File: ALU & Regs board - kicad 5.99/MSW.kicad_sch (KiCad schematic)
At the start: 8 parts, among them U12 MC74ACT04DG, U19 MC74ACT08DG, U23 MC74ACT74DG, U24 MC74ACT74DG, U25 MC74ACT244DWG, U26 MC74ACT273DWG, U27 MC74ACT157DG, U28 MC74ACT244DWG

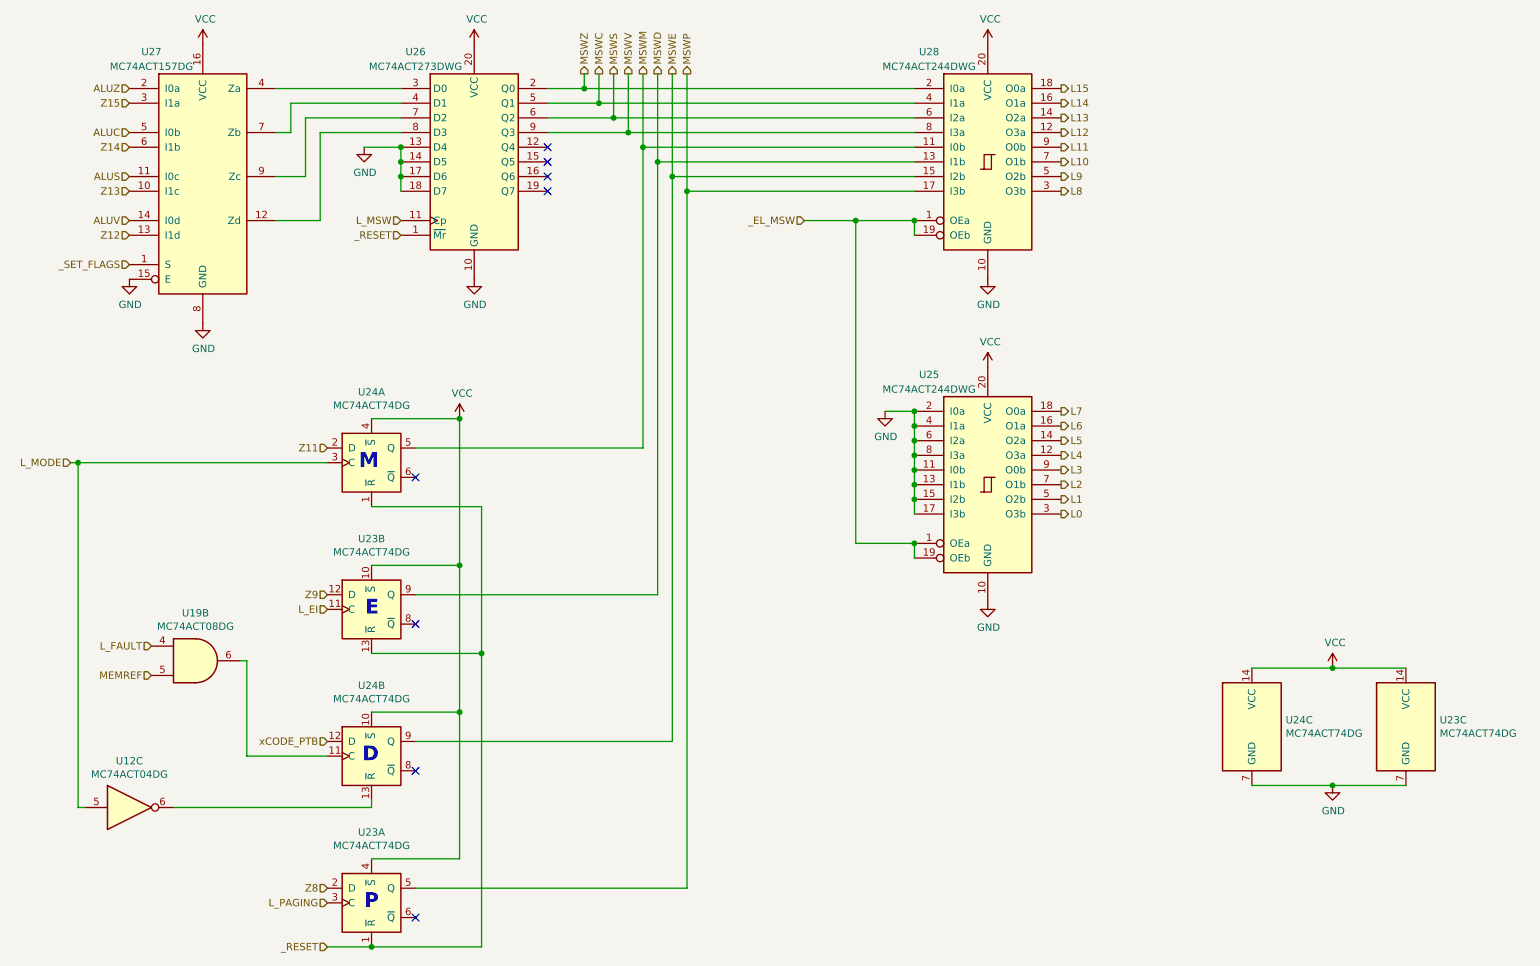
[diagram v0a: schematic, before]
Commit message: added a buffer on the _RESET line, which is rather loaded
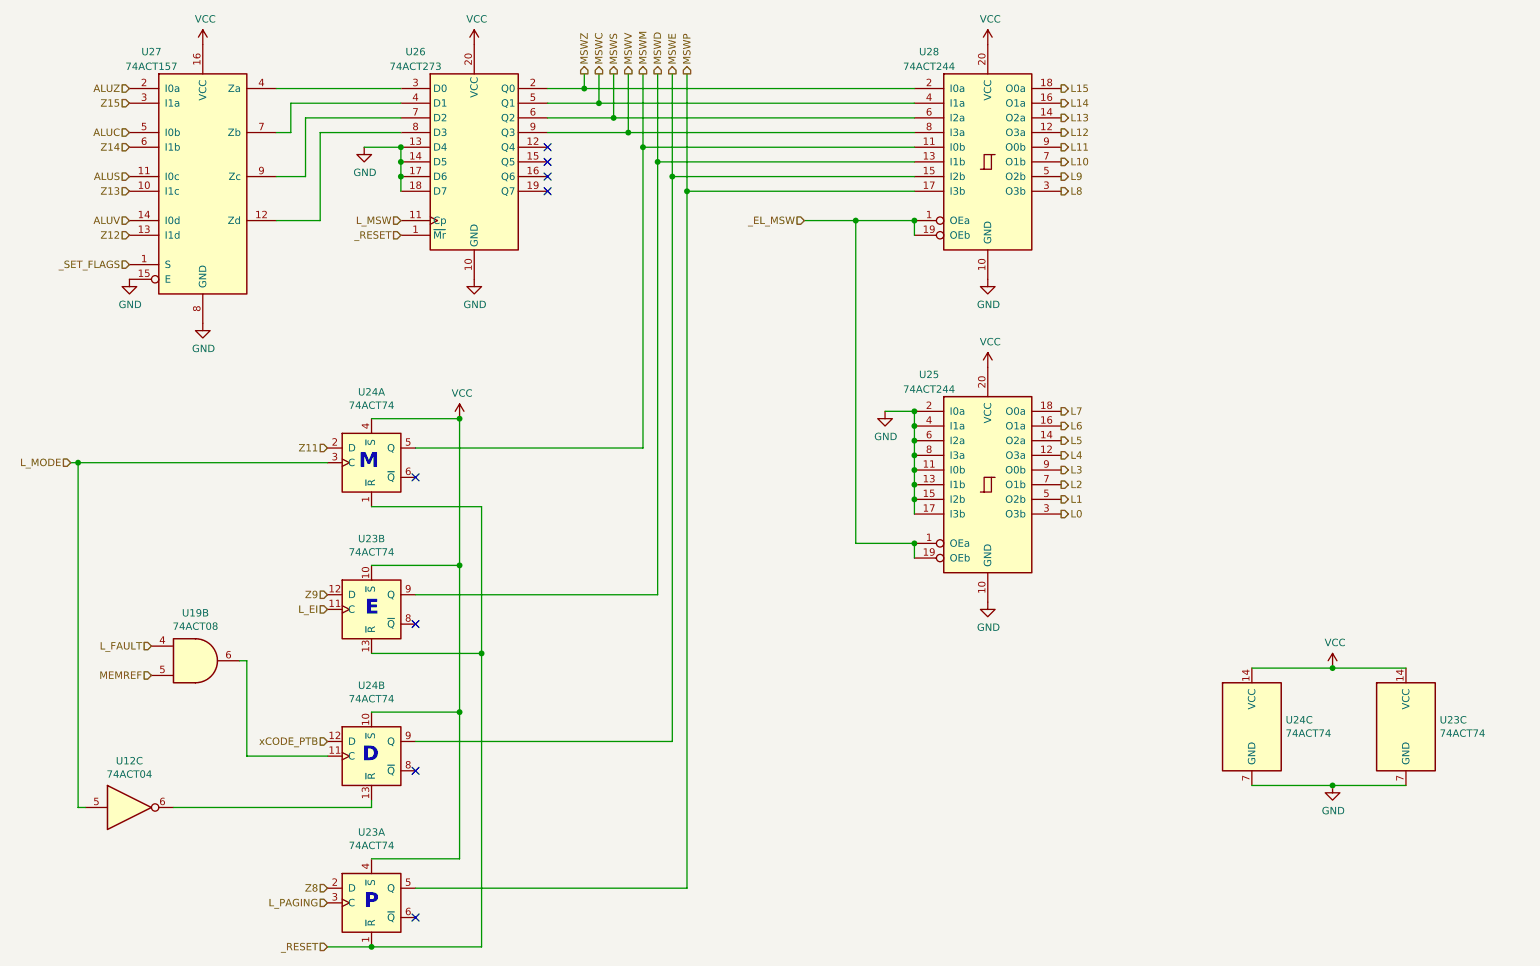
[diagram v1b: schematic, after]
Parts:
- U12: value MC74ACT04DG -> 74ACT04
- U19: value MC74ACT08DG -> 74ACT08
- U23, U24: value MC74ACT74DG -> 74ACT74
- U25, U28: value MC74ACT244DWG -> 74ACT244
- U26: value MC74ACT273DWG -> 74ACT273
- U27: value MC74ACT157DG -> 74ACT157
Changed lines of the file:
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@@
   (junction (at 245.11 134.62) (diameter 1.016) (color 0 0 0 0))
   (junction (at 245.11 154.94) (diameter 1.016) (color 0 0 0 0))
-  (no_connect (at 86.36 127))
+  (no_connect (at 86.36 152.4))
+  (no_connect (at 109.22 46.99))
+  (no_connect (at 109.22 49.53))
   (no_connect (at 109.22 44.45))
-  (no_connect (at 109.22 52.07))
-  (no_connect (at 109.22 49.53))
   (no_connect (at 86.36 101.6))
   (no_connect (at 86.36 177.8))
-  (no_connect (at 109.22 46.99))
-  (no_connect (at 86.36 152.4))
+  (no_connect (at 109.22 52.07))
+  (no_connect (at 86.36 127))
   (wire (pts (xy 27.94 99.06) (xy 26.67 99.06))
     (stroke (width 0) (type solid) (color 0 0 0 0))
@@
     (in_bom yes) (on_board yes)
     (property "Reference" "U12" (id 0) (at 36.83 150.6982 0))
-    (property "Value" "MC74ACT04DG" (id 1) (at 36.83 153.0096 0))
+    (property "Value" "74ACT04" (id 1) (at 36.83 153.01 0))
     (property "Footprint" "Package_SO:SOIC-14_3.9x8.7mm_P1.27mm" (id 2) (at 36.83 158.75 0)
       (effects (font (size 1.27 1.27)) hide)
@@
     (in_bom yes) (on_board yes)
     (property "Reference" "U19" (id 0) (at 48.26 125.095 0))
-    (property "Value" "MC74ACT08DG" (id 1) (at 48.26 127.4064 0))
+    (property "Value" "74ACT08" (id 1) (at 48.26 127.406 0))
     (property "Footprint" "Package_SO:SOIC-14_3.9x8.7mm_P1.27mm" (id 2) (at 48.26 133.35 0)
       (effects (font (size 1.27 1.27)) hide)
@@
       (effects (font (size 1.27 1.27)) (justify left))
     )
-    (property "Value" "MC74ACT74DG" (id 1) (at 236.982 145.923 0)
+    (property "Value" "74ACT74" (id 1) (at 236.982 145.923 0)
       (effects (font (size 1.27 1.27)) (justify left))
     )
@@
       (effects (font (size 1.27 1.27)) (justify left))
     )
-    (property "Value" "MC74ACT74DG" (id 1) (at 263.652 145.923 0)
+    (property "Value" "74ACT74" (id 1) (at 263.652 145.923 0)
       (effects (font (size 1.27 1.27)) (justify left))
     )
@@
     (in_bom yes) (on_board yes)
     (property "Reference" "U24" (id 0) (at 78.74 86.8426 0))
-    (property "Value" "MC74ACT74DG" (id 1) (at 78.74 89.154 0))
+    (property "Value" "74ACT74" (id 1) (at 78.74 89.154 0))
     (property "Footprint" "Package_SO:SOIC-14_3.9x8.7mm_P1.27mm" (id 2) (at 78.74 99.06 0)
       (effects (font (size 1.27 1.27)) hide)
@@
     (in_bom yes) (on_board yes)
     (property "Reference" "U23" (id 0) (at 78.74 112.2426 0))
-    (property "Value" "MC74ACT74DG" (id 1) (at 78.74 114.554 0))
+    (property "Value" "74ACT74" (id 1) (at 78.74 114.554 0))
     (property "Footprint" "Package_SO:SOIC-14_3.9x8.7mm_P1.27mm" (id 2) (at 78.74 124.46 0)
       (effects (font (size 1.27 1.27)) hide)
@@
     (in_bom yes) (on_board yes)
     (property "Reference" "U24" (id 0) (at 78.74 137.6426 0))
-    (property "Value" "MC74ACT74DG" (id 1) (at 78.74 139.954 0))
+    (property "Value" "74ACT74" (id 1) (at 78.74 139.954 0))
     (property "Footprint" "Package_SO:SOIC-14_3.9x8.7mm_P1.27mm" (id 2) (at 78.74 149.86 0)
       (effects (font (size 1.27 1.27)) hide)
@@
     (in_bom yes) (on_board yes)
     (property "Reference" "U23" (id 0) (at 78.74 163.0426 0))
-    (property "Value" "MC74ACT74DG" (id 1) (at 78.74 165.354 0))
+    (property "Value" "74ACT74" (id 1) (at 78.74 165.354 0))
     (property "Footprint" "Package_SO:SOIC-14_3.9x8.7mm_P1.27mm" (id 2) (at 78.74 175.26 0)
       (effects (font (size 1.27 1.27)) hide)
@@
     (in_bom yes) (on_board yes)
     (property "Reference" "U26" (id 0) (at 86.36 27.94 0))
-    (property "Value" "MC74ACT273DWG" (id 1) (at 86.36 30.48 0))
+    (property "Value" "74ACT273" (id 1) (at 86.36 30.48 0))
     (property "Footprint" "Package_SO:SOIC-20W_7.5x12.8mm_P1.27mm" (id 2) (at 96.52 46.99 0)
       (effects (font (size 1.27 1.27)) hide)
@@
     (in_bom yes) (on_board yes)
     (property "Reference" "U28" (id 0) (at 175.26 27.94 0))
-    (property "Value" "MC74ACT244DWG " (id 1) (at 175.26 30.48 0))
+    (property "Value" "74ACT244" (id 1) (at 175.26 30.48 0))
     (property "Footprint" "Package_SO:SOIC-20W_7.5x12.8mm_P1.27mm" (id 2) (at 185.42 46.99 0)
       (effects (font (size 1.27 1.27)) hide)
@@
     (in_bom yes) (on_board yes)
     (property "Reference" "U25" (id 0) (at 175.26 83.82 0))
-    (property "Value" "MC74ACT244DWG " (id 1) (at 175.26 86.36 0))
+    (property "Value" "74ACT244" (id 1) (at 175.26 86.36 0))
     (property "Footprint" "Package_SO:SOIC-20W_7.5x12.8mm_P1.27mm" (id 2) (at 185.42 102.87 0)
       (effects (font (size 1.27 1.27)) hide)
@@
     (in_bom yes) (on_board yes)
     (property "Reference" "U27" (id 0) (at 40.64 27.94 0))
-    (property "Value" "MC74ACT157DG" (id 1) (at 40.64 30.48 0))
+    (property "Value" "74ACT157" (id 1) (at 40.64 30.48 0))
     (property "Footprint" "Package_SO:SOIC-16_3.9x9.9mm_P1.27mm" (id 2) (at 49.53 49.53 0)
       (effects (font (size 1.27 1.27)) hide)
